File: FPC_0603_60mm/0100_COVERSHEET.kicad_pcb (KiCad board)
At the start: 2 copper layers, 66 x 7.5 mm, 1 part, among them J101 734150991

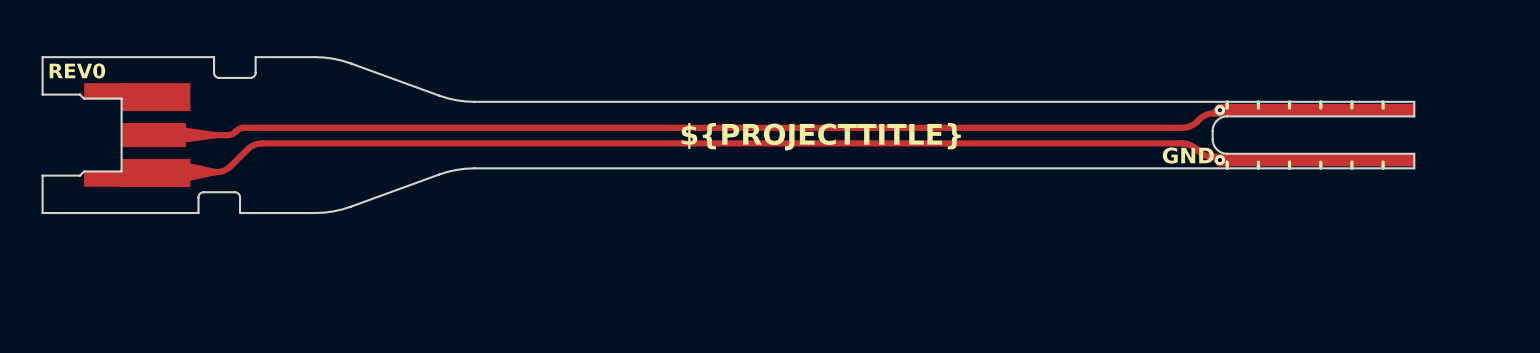
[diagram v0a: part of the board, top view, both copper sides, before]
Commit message: Regenerated outputs. Resized stiffner of -2 and -3 versions to make equal to -1 (standard)
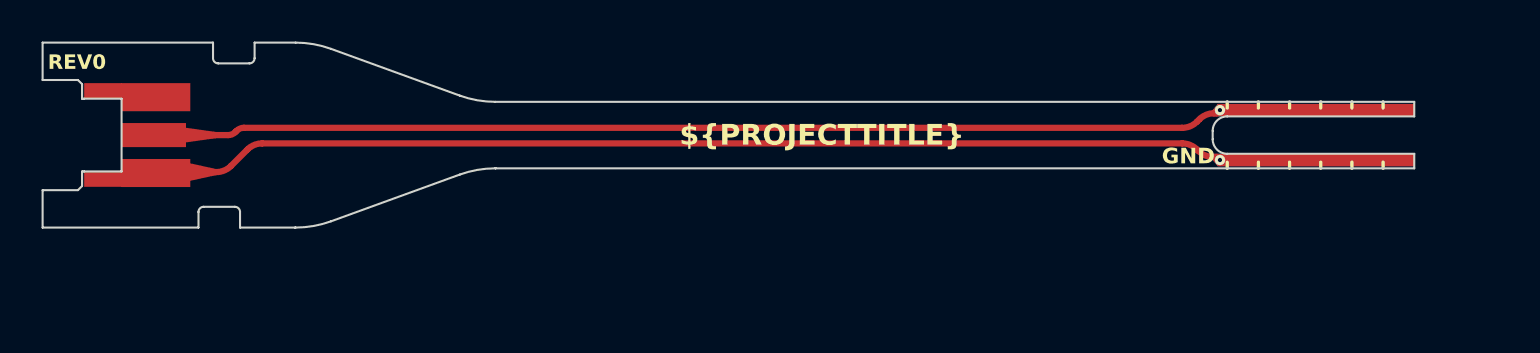
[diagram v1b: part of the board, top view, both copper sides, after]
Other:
- board size 66 x 7.5 mm -> 66 x 8.9 mm
